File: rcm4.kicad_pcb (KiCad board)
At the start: 4 copper layers, 140 x 70 mm, 159 parts, among them Y1 8MHz, Y2 32.768kHz

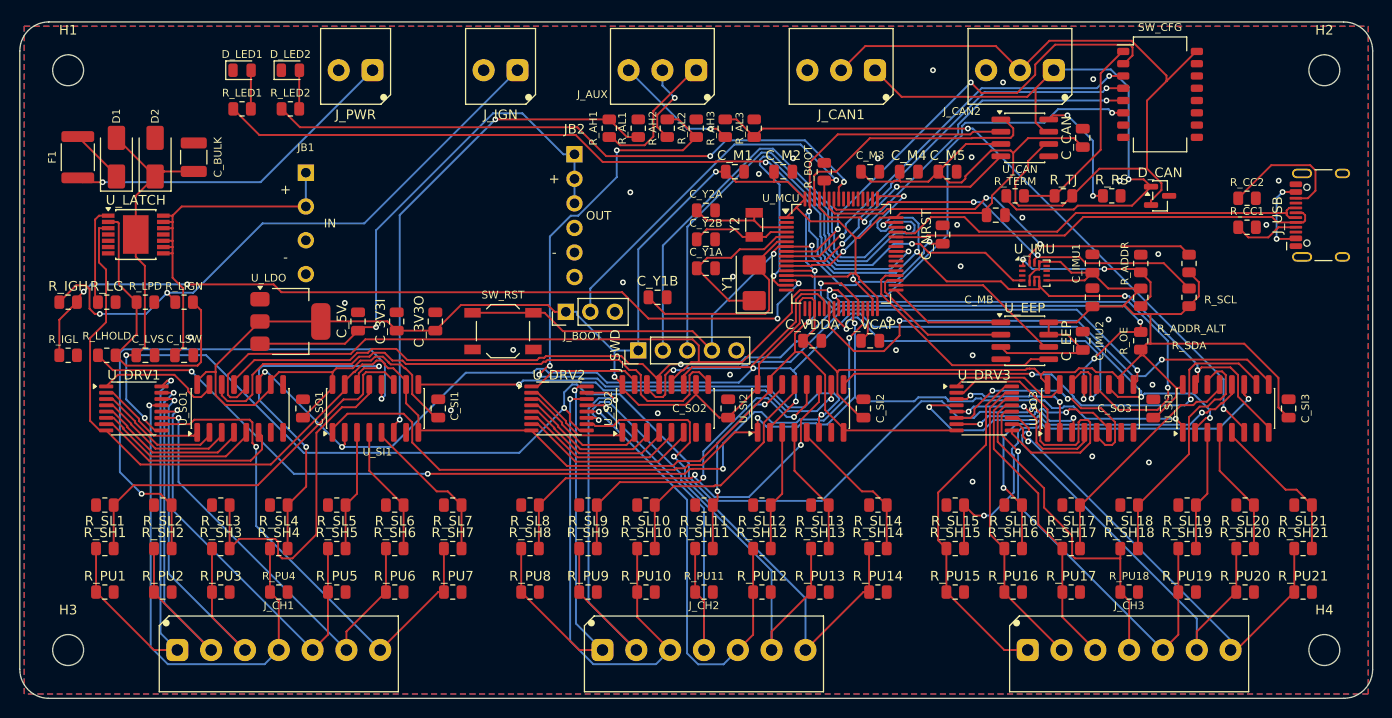
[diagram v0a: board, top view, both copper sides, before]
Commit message: rcm: FIX D1 wired backwards - board would never have powered up
Diode:SS34 uses KiCad's pin 1 = K, pin 2 = A convention, not the
pin-1-is-anode you would assume. The netlist had D1.1 (cathode) on
+12V_FUSED and D1.2 (anode) on +12V_P, putting the reverse-polarity diode
in backwards. It would have blocked the battery feed outright.

Found by the user reading the schematic symbol and noticing the cathode
bar pointed at the fuse.

Nothing automated caught this and nothing was going to: ERC passes either
orientation because a diode is a valid two-pin connection both ways, and
DRC, the netlist round-trip and the BOM are all equally blind. Same class
as the four faults found in the first schematic review - correct
connectivity, wrong circuit.

Audited the other polarised parts while here; all correct. D_LED1/2 have
anode on pin 2 to the resistor and cathode on pin 1 to GND. D2 works out
right because D_SMA's pad 1 is the cathode and sits on +12V_P - though
Device:D_TVS is a BIDIRECTIONAL symbol standing in for a unidirectional
SMAJ33A, so the schematic cannot express that polarity. Worth swapping
for a directional symbol if revised.

BOTH BOARDS AND BOTH MFG SETS ARE NOW STALE - built from the wrong
circuit, and must be rebuilt and re-routed before anything is ordered.

Co-Authored-By: Claude Opus 5 <noreply@anthropic.com>
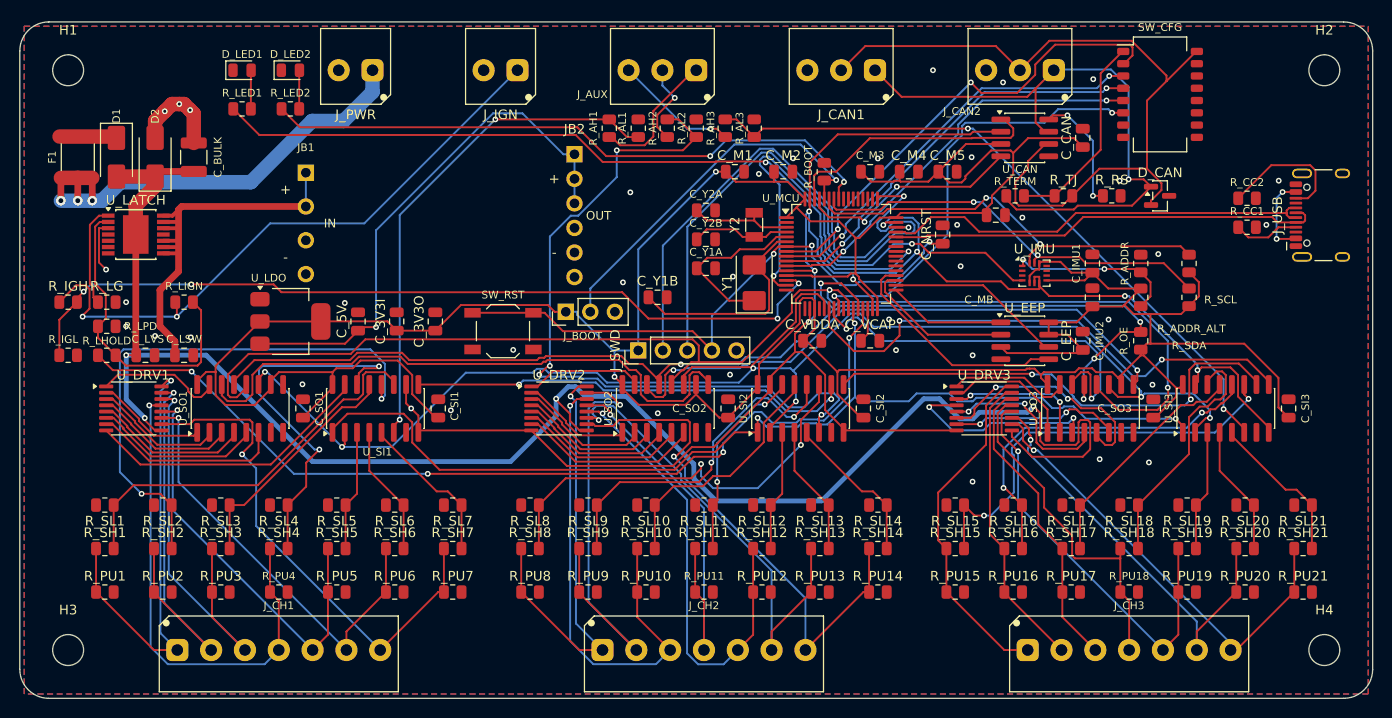
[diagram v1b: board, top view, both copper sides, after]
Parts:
- moved R_LPD 4.72 mm to (9.00, 31.5)
- turned D1 to -90 degrees
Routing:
- net GND: track 264.1 -> 246.7 mm, vias 39 -> 48
- net +12V_IN: track 35.5 -> 49.5 mm, vias 1 -> 3
- net SNS3: track 35.1 -> 24.7 mm
- net +12V_SW: track 38.7 -> 43.0 mm
- net LATCH_IGN: track 62.3 -> 64.3 mm
- net SNS4: track 37.6 -> 39.0 mm
- net SNS16: track 39.4 -> 38.2 mm
- net CH9: track 46.6 -> 47.6 mm
- net SNS15: track 45.1 -> 44.1 mm
- net SNS8: track 43.3 -> 44.3 mm
- net LATCH_HOLD: track 98.3 -> 97.3 mm
- net CH20: track 45.7 -> 44.8 mm
- net CH7: track 52.3 -> 53.2 mm
- net DRV18: track 21.6 -> 20.9 mm

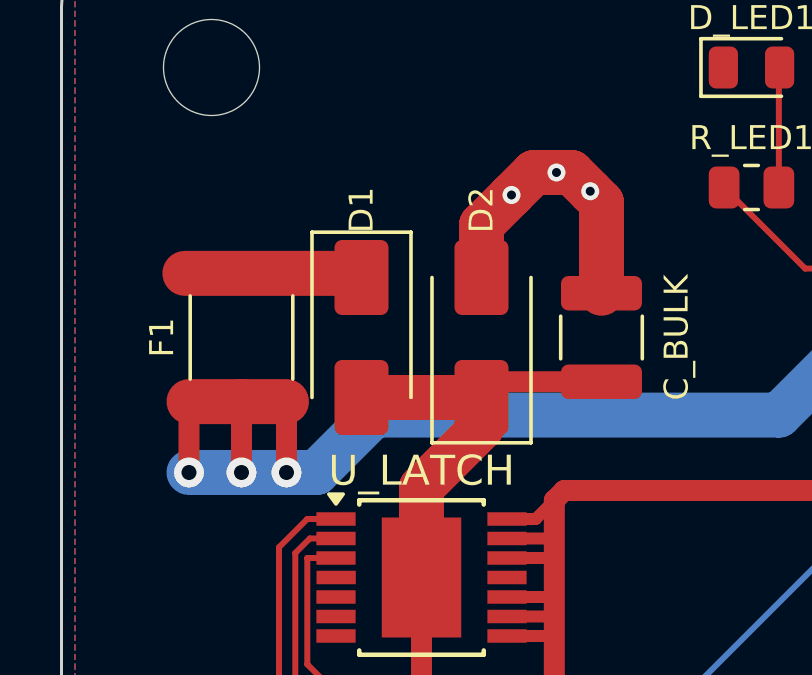
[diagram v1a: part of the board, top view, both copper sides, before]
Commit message: rcm: D1 corrected in place on both boards - no re-route needed
The netlist fix swapped which net each of D1's two pads carries. Because
D_SMA's pads are symmetric about the footprint origin, rotating the part
180 degrees lands pad 1 exactly where pad 2 was - so rotating AND
reassigning the nets together lets the existing traces arrive at the
right pads with no routing changed at all. That matters on rcm4, where
the routing has been hand-tidied and is not reproducible from a rebuild.

Both boards verified electrically rather than just DRC-clean:

  rcm4   pad2 (A) = +12V_FUSED, pad1 (K) = +12V_P
  rcm    pad2 (A) = +12V_FUSED, pad1 (K) = +12V_P

Current flows fuse -> anode -> cathode -> protected rail on both. The two
carry different D1 rotations, which is fine; both are correct.

0 unconnected, 0 schematic parity, 0 electrical violations on both. The
schematic-parity result is the real confirmation - it means each board
now matches the corrected netlist.

Manufacturing files are still stale on both and need regenerating, but
neither board needs re-routing.

Co-Authored-By: Claude Opus 5 <noreply@anthropic.com>
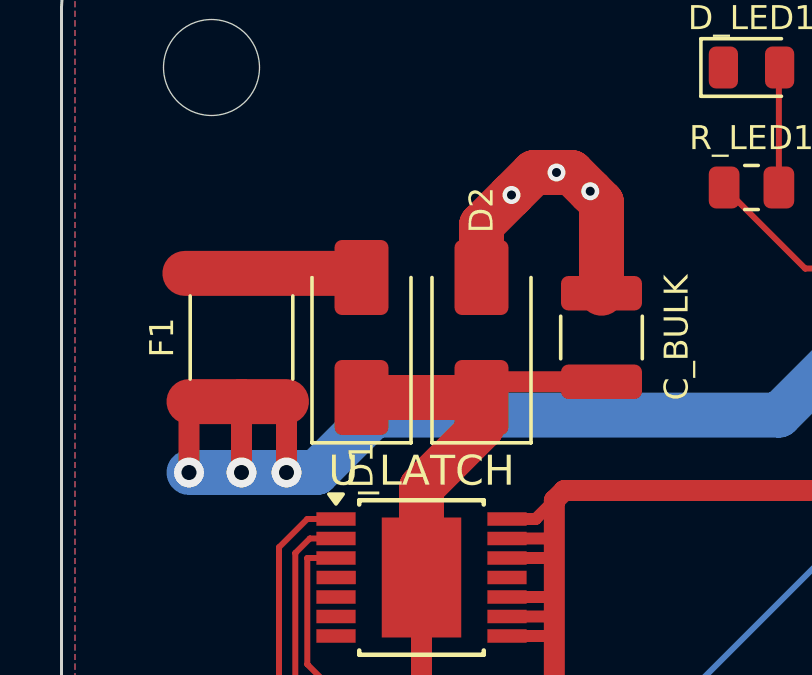
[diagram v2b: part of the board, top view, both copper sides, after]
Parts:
- turned D1 to 90 degrees
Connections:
- D1 pad 1: +12V_FUSED -> +12V_P
- D1 pad 2: +12V_P -> +12V_FUSED
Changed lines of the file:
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@@
 	(footprint "Diode_SMD:D_SMA"
 		(layer "F.Cu")
-		(at 10 14 -90)
+		(at 10 14 90)
 		(descr "Diode SMA (DO-214AC)")
 		(tags "Diode SMA (DO-214AC)")
 		(property "Reference" "D1"
-			(at -4.25 0 270)
+			(at -4.25 0 90)
 			(layer "F.SilkS")
 			(effects
@@
 		)
 		(property "Value" "SS34"
-			(at 0 2.6 270)
+			(at 0 2.6 90)
 			(layer "F.Fab")
 			(effects
@@
 		)
 		(property "Datasheet" ""
-			(at 0 0 270)
+			(at 0 0 90)
 			(unlocked yes)
 			(layer "F.Fab")
@@
 		)
 		(property "Description" ""
-			(at 0 0 270)
+			(at 0 0 90)
 			(unlocked yes)
 			(layer "F.Fab")
@@
 		(duplicate_pad_numbers_are_jumpers no)
 		(fp_line
-			(start -3.51 1.65)
-			(end 2 1.65)
+			(start -3.51 -1.65)
+			(end 2 -1.65)
 			(stroke
 				(width 0.12)
@@
 		)
 		(fp_line
-			(start -3.51 -1.65)
-			(end 2 -1.65)
+			(start -3.51 1.65)
+			(end 2 1.65)
 			(stroke
 				(width 0.12)
@@
 		)
 		(fp_line
-			(start -3.5 1.75)
-			(end -3.5 -1.75)
+			(start 3.5 -1.75)
+			(end 3.5 1.75)
 			(stroke
 				(width 0.05)
@@
 		)
 		(fp_line
-			(start 3.5 1.75)
-			(end -3.5 1.75)
+			(start -3.5 -1.75)
+			(end 3.5 -1.75)
 			(stroke
 				(width 0.05)
@@
 		)
 		(fp_line
-			(start -3.5 -1.75)
-			(end 3.5 -1.75)
+			(start 3.5 1.75)
+			(end -3.5 1.75)
 			(stroke
 				(width 0.05)
@@
 		)
 		(fp_line
-			(start 3.5 -1.75)
-			(end 3.5 1.75)
+			(start -3.5 1.75)
+			(end -3.5 -1.75)
 			(stroke
 				(width 0.05)
@@
 		)
 		(fp_line
-			(start -2.3 1.5)
+			(start 2.3 -1.5)
 			(end -2.3 -1.5)
 			(stroke
@@
 		)
 		(fp_line
-			(start 2.3 1.5)
-			(end -2.3 1.5)
+			(start 2.3 -1.5)
+			(end 2.3 1.5)
 			(stroke
 				(width 0.1)
@@
 		)
 		(fp_line
-			(start 0.50118 0.75032)
-			(end 0.50118 -0.79908)
+			(start -0.64944 -0.79908)
+			(end -0.64944 0.80112)
 			(stroke
 				(width 0.1)
@@
 		)
 		(fp_line
-			(start -0.64944 0.00102)
-			(end 0.50118 0.75032)
+			(start 0.50118 0.00102)
+			(end 1.4994 0.00102)
 			(stroke
 				(width 0.1)
@@
 		(fp_line
 			(start -0.64944 0.00102)
-			(end -1.55114 0.00102)
+			(end 0.50118 -0.79908)
 			(stroke
 				(width 0.1)
@@
 		(fp_line
 			(start -0.64944 0.00102)
-			(end 0.50118 -0.79908)
+			(end -1.55114 0.00102)
 			(stroke
 				(width 0.1)
@@
 		)
 		(fp_line
-			(start 0.50118 0.00102)
-			(end 1.4994 0.00102)
+			(start -0.64944 0.00102)
+			(end 0.50118 0.75032)
 			(stroke
 				(width 0.1)
@@
 		)
 		(fp_line
-			(start -0.64944 -0.79908)
-			(end -0.64944 0.80112)
+			(start 0.50118 0.75032)
+			(end 0.50118 -0.79908)
 			(stroke
 				(width 0.1)
@@
 		)
 		(fp_line
-			(start 2.3 -1.5)
-			(end 2.3 1.5)
+			(start 2.3 1.5)
+			(end -2.3 1.5)
 			(stroke
 				(width 0.1)
@@
 		)
 		(fp_line
-			(start 2.3 -1.5)
+			(start -2.3 1.5)
 			(end -2.3 -1.5)
 			(stroke
@@
 		)
 		(fp_text user "${REFERENCE}"
-			(at 0 -2.5 270)
+			(at 0 -2.5 90)
 			(layer "F.Fab")
 			(effects
@@
 		)
 		(pad "1" smd roundrect
-			(at -2 0 270)
+			(at -2 0 90)
 			(size 2.5 1.8)
 			(layers "F.Cu" "F.Mask" "F.Paste")
 			(roundrect_rratio 0.1388888889)
-			(net "+12V_FUSED")
+			(net "+12V_P")
 		)
 		(pad "2" smd roundrect
-			(at 2 0 270)
+			(at 2 0 90)
 			(size 2.5 1.8)
 			(layers "F.Cu" "F.Mask" "F.Paste")
 			(roundrect_rratio 0.1388888889)
-			(net "+12V_P")
+			(net "+12V_FUSED")
 		)
 		(embedded_fonts no)
@@
 	)
 	(segment
-		(start 9.8625 11.8625)
-		(end 10 12)
-		(width 1.5)
-		(layer "F.Cu")
-		(net "+12V_FUSED")
-	)
-	(segment
-		(start 4.1125 11.8625)
-		(end 9.8625 11.8625)
-		(width 1.5)
-		(layer "F.Cu")
-		(net "+12V_FUSED")
-	)
-	(segment
 		(start 10 16)
 		(end 14 16)
@@
 	)
 	(segment
+		(start 9.8625 11.8625)
+		(end 10 12)
+		(width 1.5)
+		(layer "F.Cu")
+		(net "+12V_FUSED")
+	)
+	(segment
+		(start 4.1125 11.8625)
+		(end 9.8625 11.8625)
+		(width 1.5)
+		(layer "F.Cu")
+		(net "+12V_FUSED")
+	)
+	(segment

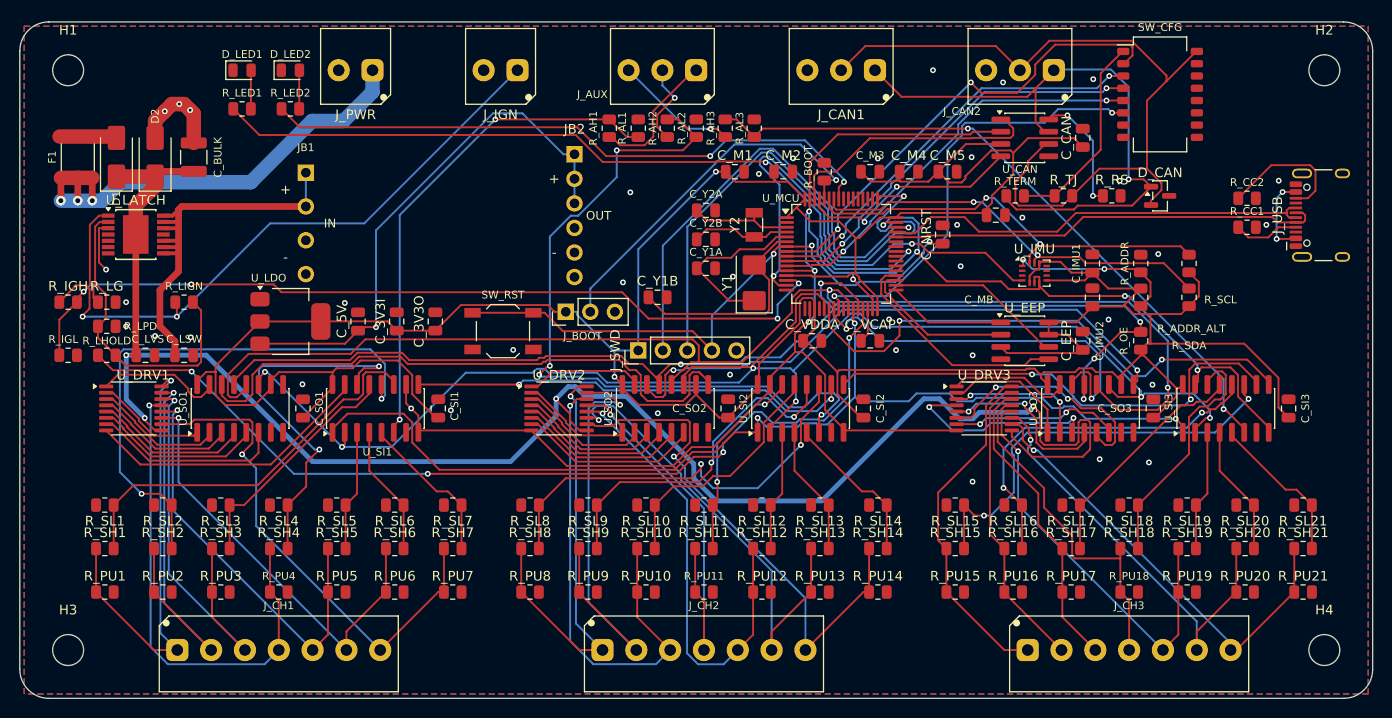
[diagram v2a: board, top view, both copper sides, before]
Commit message: rcm4 READY: 0 violations of any kind, manufacturing set regenerated
Final state of the 4-layer board after the user's trace tidy-up and the
D1 correction:

  0 DRC violations - not just electrical, silkscreen too
  0 unconnected, 0 schematic parity
  4 zones, 189 vias, 1765 segments

mfg4/ regenerated: 16 gerbers, BOM 43 lines all sourced, CPL 152
placements. Both planes export as a SINGLE filled region, silkscreen has
no pad flashes or clear-polarity blocks, outline exactly 140.00x70.00mm.

Re-inserted the stackup, which KiCad had discarded when the board was
saved from the GUI - almost certainly because my block named the inner
layers In1.Cu/In2.Cu while the board calls them GND_plane/PWR_plane. Now
written with the board's own names. The stackup is NOT reachable through
the pcbnew Python API (GetStackupDescriptor returns an opaque
SwigPyObject), so it can only be set by text or in Board Setup - worth
re-checking it survived if the board is saved from KiCad again.

mfg/ (2-layer) also regenerated so it is not left carrying the pre-fix D1.

Drill sizes picked up 0.4 and 0.5mm from the hand-added vias, alongside
the original 0.3/0.6/1.0/1.2. All within the 0.3mm minimum already
selected on the order form.

Co-Authored-By: Claude Opus 5 <noreply@anthropic.com>
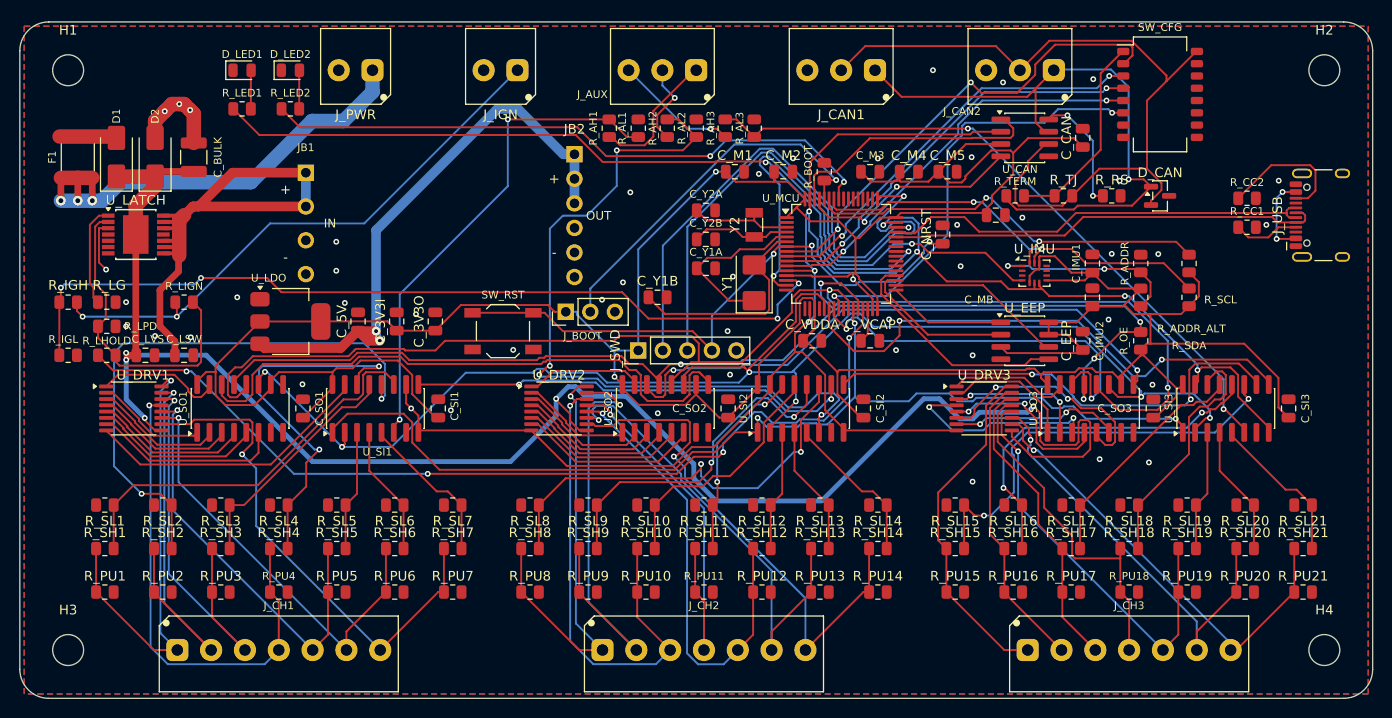
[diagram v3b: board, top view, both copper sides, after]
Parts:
- turned R_IGH to 180 degrees
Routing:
- net +12V_SW: track 43.0 -> 58.2 mm
- net LATCH_IGN: track 64.3 -> 58.9 mm
- net +5V: track 55.1 -> 60.5 mm, vias 1 -> 2
- net IGN_SENSE: track 87.2 -> 89.3 mm
- net IMU_SDO: track 17.8 -> 19.8 mm
- net SNS2: track 57.0 -> 58.4 mm
- net GND: track 246.7 -> 245.6 mm, vias 48 -> 55
- net ASNS2: track 77.5 -> 78.5 mm
- net +12V_P: track 182.0 -> 182.9 mm, vias 4 -> 5
- net +3V3: track 384.3 -> 385.2 mm
- net IMU_SCL: track 42.7 -> 43.5 mm
- net ASNS1: track 52.3 -> 51.5 mm
- net SR_RCLK: track 135.3 -> 135.8 mm
